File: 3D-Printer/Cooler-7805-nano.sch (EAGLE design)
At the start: 36 parts, among them IC1 L293D, IC2 REG1117

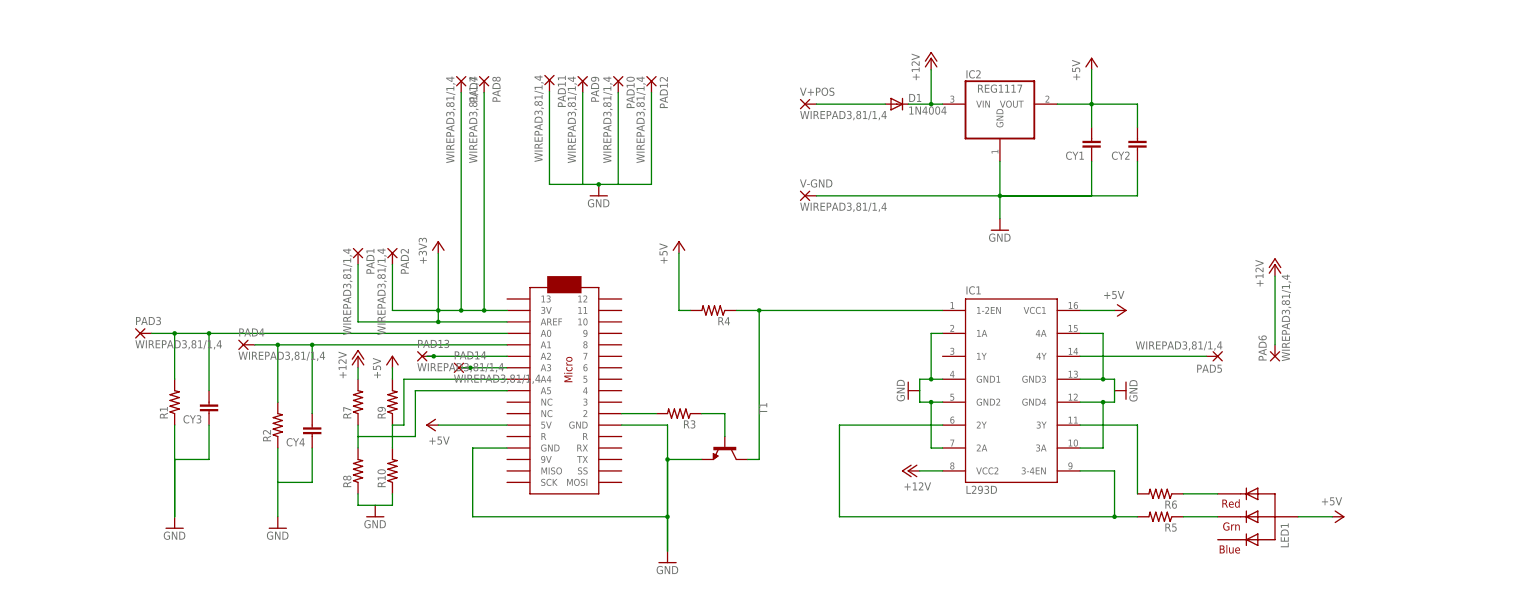
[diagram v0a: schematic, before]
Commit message: correct meters
meters and serial needed reversed.
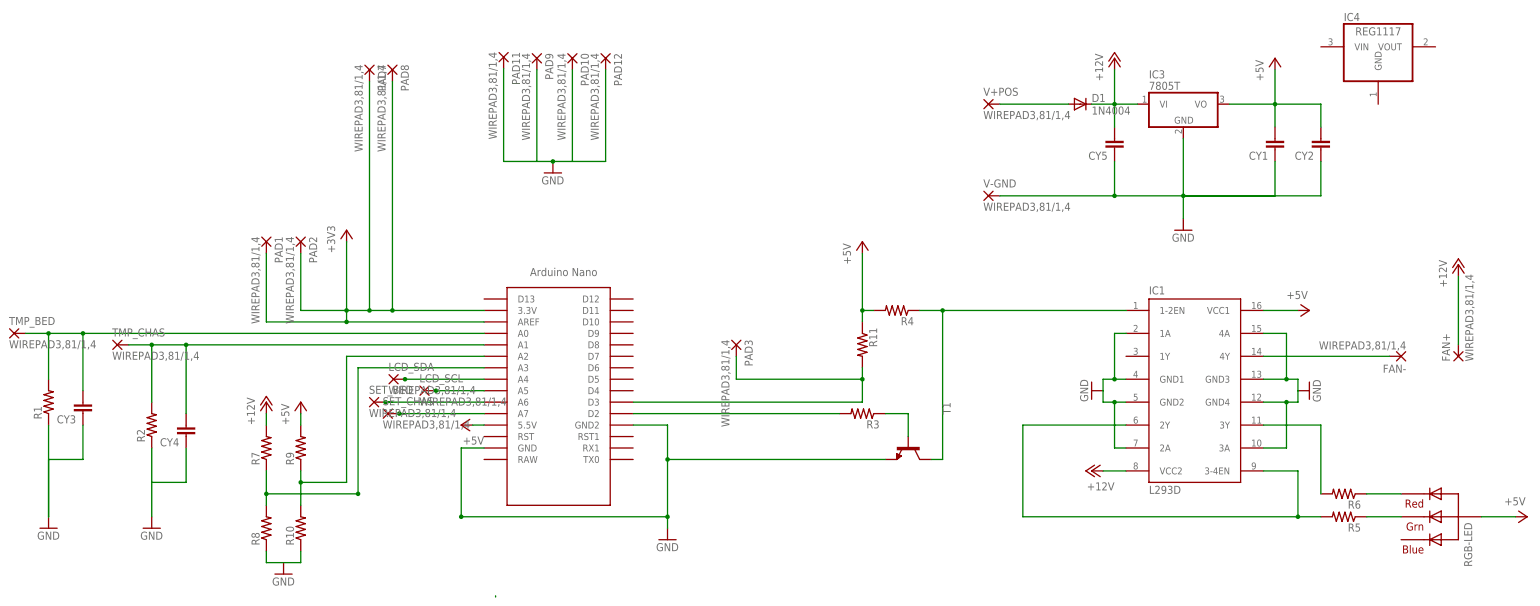
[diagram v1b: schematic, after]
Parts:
- removed IC2: REG1117, burr-brown:REG1117
- removed LED1: RGBLED_CA-5MM, adafruit:RGBLED_CA-5MM
- removed PAD13, PAD14, PAD4, PAD5, PAD6: WIREPAD3,81/1,4, wirepad:WIREPAD3,81/1,4
- removed U$1: ARDUINOMICRO, adafruit:ARDUINOMICRO
- added CY5: (no value), resistor:CYYC7B5
- added FAN+, FAN-, LCD_SCL, LCD_SDA, SET_BED, SET_CHAS, TMP_BED, TMP_CHAS: WIREPAD3,81/1,4, wirepad:WIREPAD3,81/1,4
- added IC3: 7805T, adafruit:7805T
- added IC4: REG1117, burr-brown:REG1117
- added R11: (no value), adafruit:R-US_0309/10
- added RGB-LED: RGBLED_CA-5MM, adafruit:RGBLED_CA-5MM
- added U$2: NANO, Arduino-clone:NANO
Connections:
- removed net N$2: R3.2, U$1.2
- removed net N$23: PAD13.P, U$1.A2
- removed net N$24: PAD14.P, U$1.A3
- new net N$14: R3.2, U$2.D2
- new net N$18: SET_BED.P, U$2.A6
- new net N$19: PAD3.P, R11.2, U$2.D3
- new net N$20: R7.1, R8.2, U$2.A3
- new net N$44: LCD_SDA.P, U$2.A4
- new net N$45: LCD_SCL.P, U$2.A5
- net +12V: now also CY5.2, FAN+.P, IC3.VI; no longer IC2.VIN, PAD6.P
- net +3V3: now also U$2.3.3V, U$2.AREF; no longer U$1.3V, U$1.AREF
- net +5V: now also IC3.VO, R11.1, RGB-LED.VCC, U$2.5.5V; no longer IC2.VOUT, LED1.VCC, U$1.5V
- net GND: now also CY5.1, IC3.GND, U$2.GND, U$2.GND2; no longer IC2.GND, U$1.GND, U$1.GND@1
- net N$10: now also RGB-LED.GREEN; no longer LED1.GREEN
- net N$11: now also FAN-.P; no longer PAD5.P
- net N$25: now also R10.2, R9.1, U$2.A2; no longer R7.1, R8.2, U$1.A5
- net N$26: now also SET_CHAS.P, U$2.A7; no longer R10.2, R9.1, U$1.A4
- net N$4: now also TMP_BED.P, U$2.A0; no longer PAD3.P, U$1.A0
- net N$6: now also TMP_CHAS.P, U$2.A1; no longer PAD4.P, U$1.A1
- net N$9: now also RGB-LED.RED; no longer LED1.RED
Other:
- moved on the sheet: CY1, CY2, CY3, CY4, D1, IC1, PAD1, PAD10, PAD11, PAD12, PAD2, PAD3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

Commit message: Added bounce capacitor
Corrected bounce on switch
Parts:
- added CY6: (no value), resistor:CYYC7B5
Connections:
- net +5V: now also CY6.2
- net N$19: now also CY6.1
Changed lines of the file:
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@@
 <part name="SET_BED" library="wirepad" deviceset="WIREPAD" device="3,81/1,4"/>
 <part name="SET_CHAS" library="wirepad" deviceset="WIREPAD" device="3,81/1,4"/>
+<part name="CY6" library="resistor" deviceset="CY" device="YC7B5"/>
 </parts>
 <sheets>
@@
 <instance part="SET_BED" gate="G$1" x="11.176" y="63.5"/>
 <instance part="SET_CHAS" gate="G$1" x="14.224" y="60.96"/>
+<instance part="CY6" gate="G$1" x="111.76" y="73.66" rot="R180"/>
 </instances>
 <busses>
@@
 <pinref part="R11" gate="G$1" pin="1"/>
 <wire x1="119.38" y1="81.28" x2="119.38" y2="83.82" width="0.1524" layer="91"/>
+<pinref part="CY6" gate="G$1" pin="2"/>
+<wire x1="111.76" y1="78.74" x2="111.76" y2="83.82" width="0.1524" layer="91"/>
+<wire x1="111.76" y1="83.82" x2="119.38" y2="83.82" width="0.1524" layer="91"/>
 </segment>
 <segment>
@@
 <junction x="119.38" y="68.58"/>
 <wire x1="119.38" y1="68.58" x2="119.38" y2="71.12" width="0.1524" layer="91"/>
-<wire x1="119.38" y1="68.58" x2="91.44" y2="68.58" width="0.1524" layer="91"/>
+<wire x1="111.76" y1="68.58" x2="91.44" y2="68.58" width="0.1524" layer="91"/>
 <wire x1="91.44" y1="68.58" x2="91.44" y2="73.66" width="0.1524" layer="91"/>
 <pinref part="PAD3" gate="G$1" pin="P"/>
 <pinref part="U$2" gate="G$1" pin="D3"/>
-</segment>
-</net>
+<pinref part="CY6" gate="G$1" pin="1"/>
+<wire x1="111.76" y1="71.12" x2="111.76" y2="68.58" width="0.1524" layer="91"/>
+<wire x1="111.76" y1="68.58" x2="119.38" y2="68.58" width="0.1524" layer="91"/>
+</segment>
+</net>
